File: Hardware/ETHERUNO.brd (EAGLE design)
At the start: 68.6 x 53.3 mm, 99 parts, among them IC1 MC33269DT-5.0, IC2 ATMEGA16U2-MU, IC3 ATMEGA328P TQFP32, IC4 LM358D, IC5 W5500-LQFP, IC6 MCP24AA025E48, J1 Digital_8_13, J10 ICSP:USB, J11 microSD, J2 Power, J3 Analog, J4 Digital_0_7, J5 DC_2_1MM, J6 USB-C-16P-16P, J7 INT, J8 FT-POE-MODULE3, J9 ICSP:MAIN, Q1 FDN340P, Q2 2N7002, U1 HY931147C-RJ45

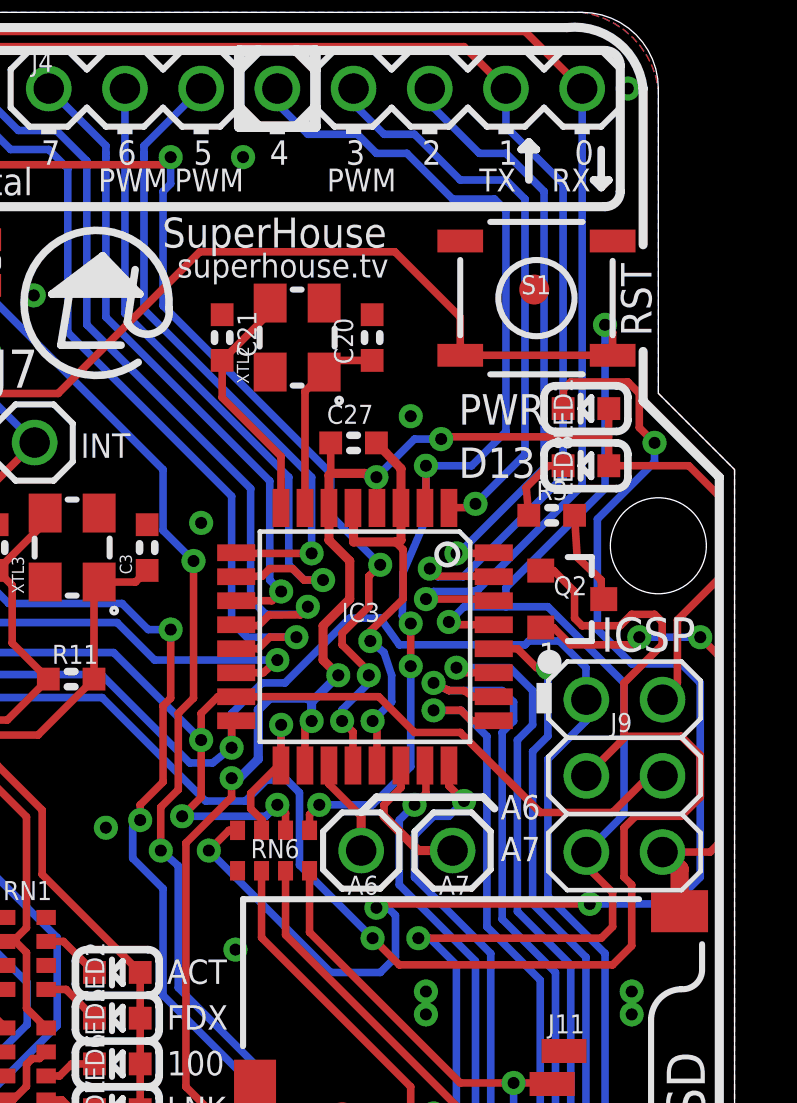
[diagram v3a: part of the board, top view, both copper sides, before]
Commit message: Added cut-track jumper to isolate D4 from SD_CS
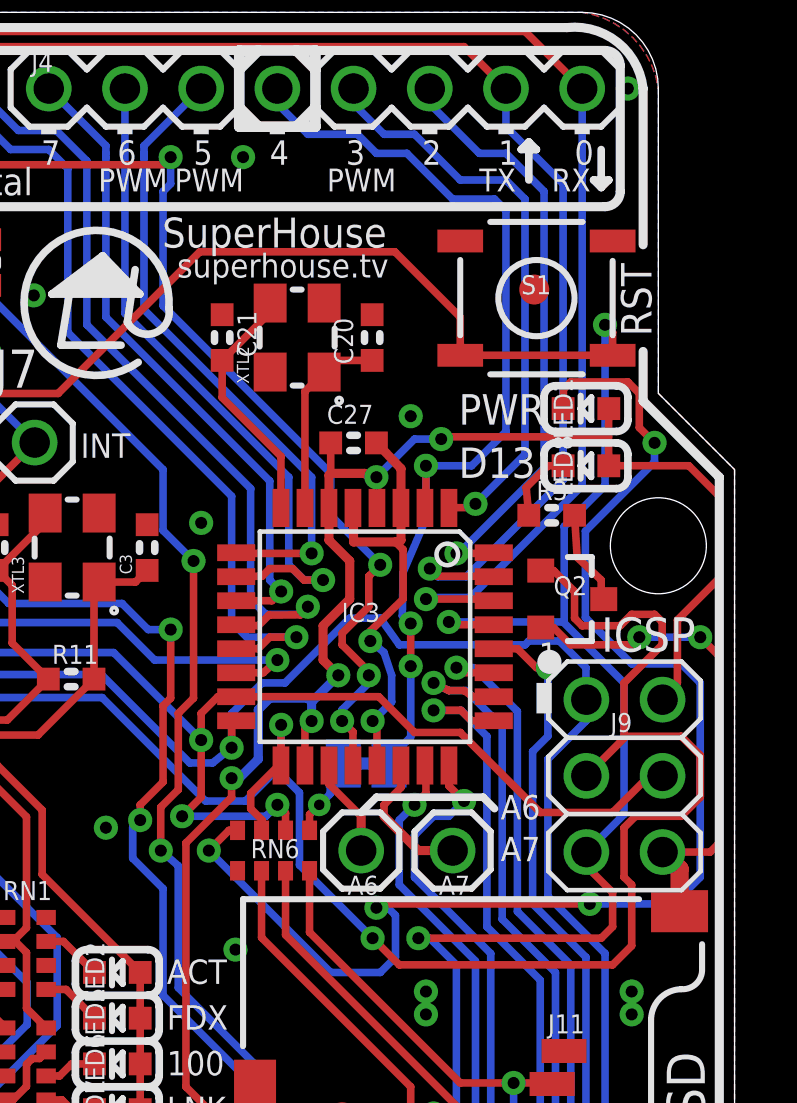
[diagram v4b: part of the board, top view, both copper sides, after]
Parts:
- added U$2: SJC-NORMAL, SuperHouse-Jumpers:SJC
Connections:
- new net N$44: RN6.5, U$2.1
- net D4: now also U$2.2; no longer RN6.5
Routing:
- net D4: track 36.4 -> 32.3 mm, vias 4 -> 3
- net N$44: track 0.00 -> 2.69 mm, vias 0 -> 1
- net A4_SDA: track 124.3 -> 123.2 mm
- net A3: track 35.5 -> 34.4 mm
- net RESET: track 127.0 -> 126.3 mm
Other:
- board text added: "D4"
